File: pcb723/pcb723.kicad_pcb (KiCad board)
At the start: 4 copper layers, 90 x 70 mm, 71 parts, among them J1 Conn_01x02_Pin, J10 Conn_01x05_Socket, J11 Conn_01x05_Socket, J2 Conn_01x02_Pin, J3 Conn_02x07_Odd_Even, J4 Conn_02x02_Odd_Even, J5 USB_C_Receptacle_USB2.0_16P, J6 Conn_02x13_Odd_Even, J7 Conn_02x14_Odd_Even, J8 Conn_02x13_Odd_Even, J9 Conn_02x12_Odd_Even, SW1 SW_Push, U1 STM32H723ZGT6, U2 AMS1117-3.3, Y1 8MHz 20pF

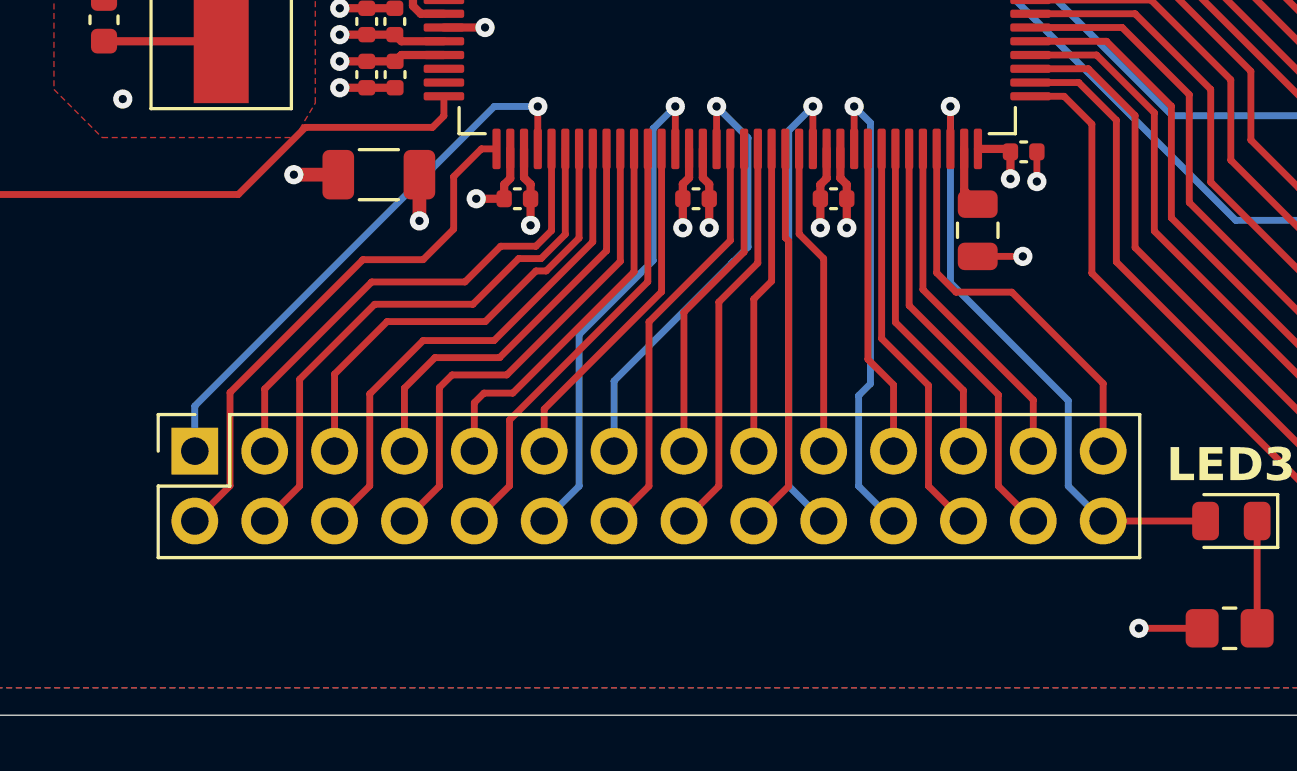
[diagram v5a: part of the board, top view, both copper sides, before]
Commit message: LED3 labels
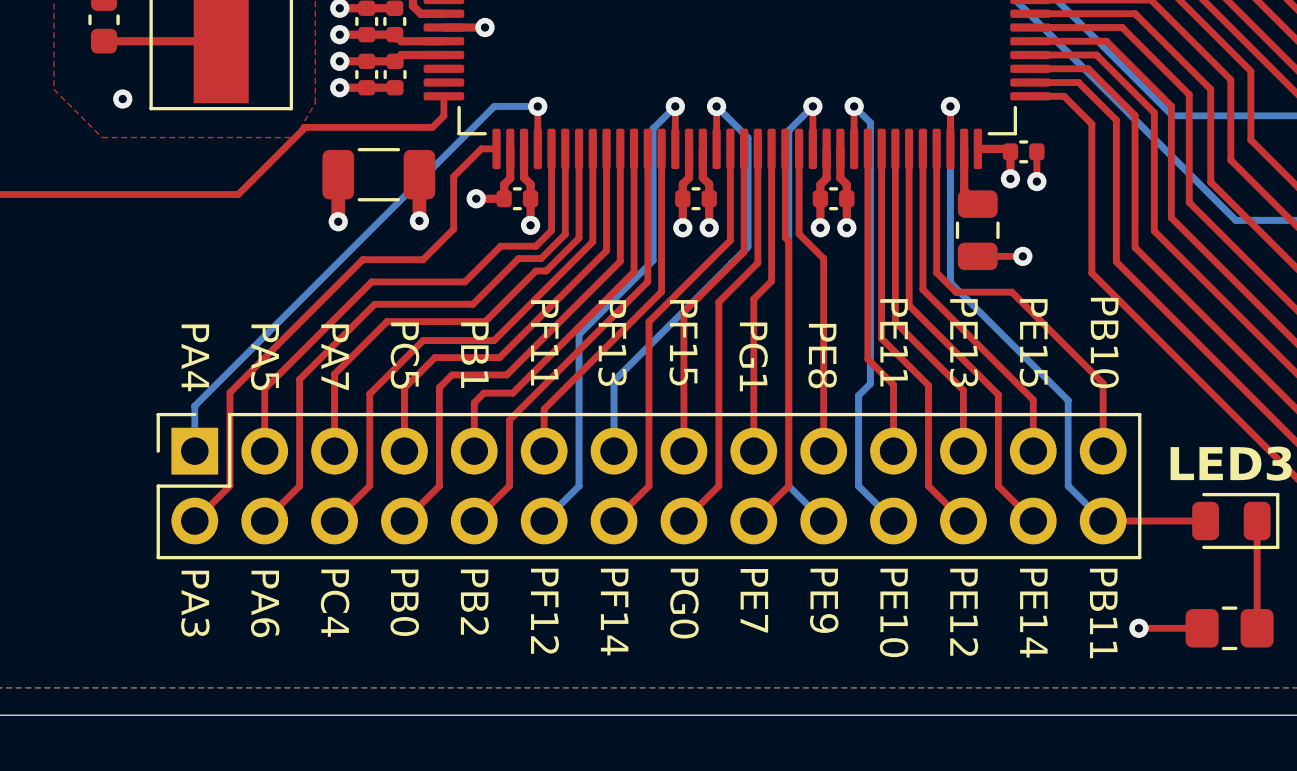
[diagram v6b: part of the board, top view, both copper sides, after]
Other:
- board text added: "PA3"
- board text added: "PA4"
- board text added: "PA5"
- board text added: "PA6"
- board text added: "PA7"
- board text added: "PB0"
- board text added: "PB1"
- board text added: "PB10"
- board text added: "PB11"
- board text added: "PB2"
- board text added: "PC4"
- board text added: "PC5"
- board text added: "PE10"
- board text added: "PE11"
- board text added: "PE12"
- board text added: "PE13"
- board text added: "PE14"
- board text added: "PE15"
- board text added: "PE7"
- board text added: "PE8"
- board text added: "PE9"
- board text added: "PF11"
- board text added: "PF12"
- board text added: "PF13"
- board text added: "PF14"
- board text added: "PF15"
- board text added: "PG0"
- board text added: "PG1"

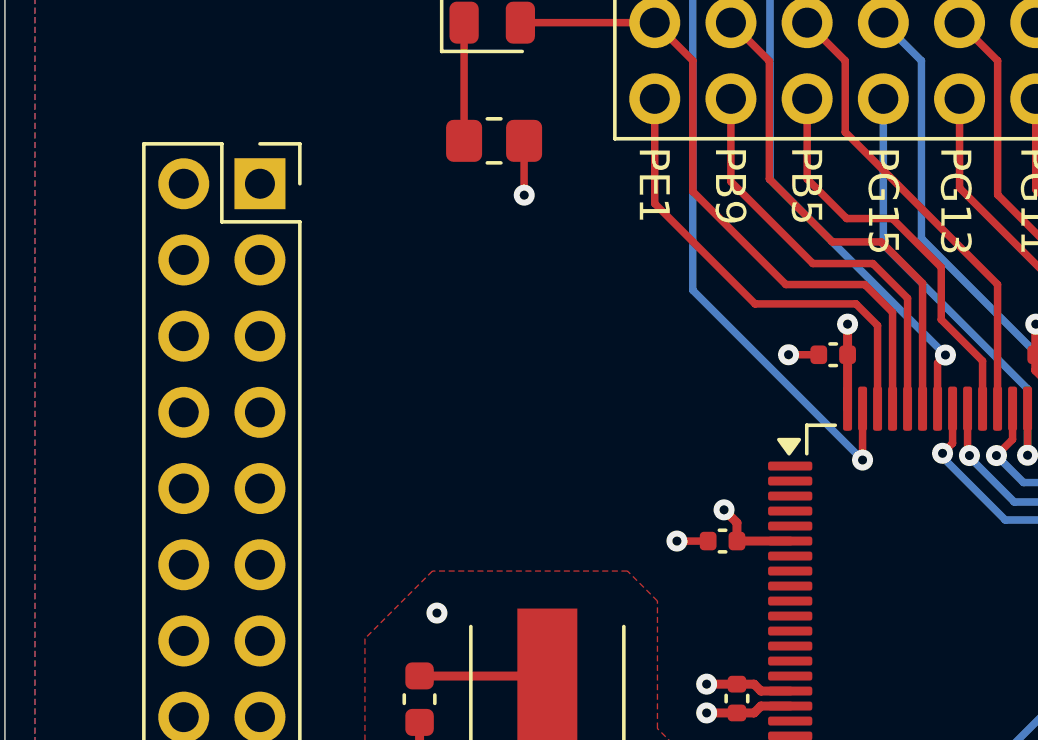
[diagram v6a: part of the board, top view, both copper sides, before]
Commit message: Route LED2 top
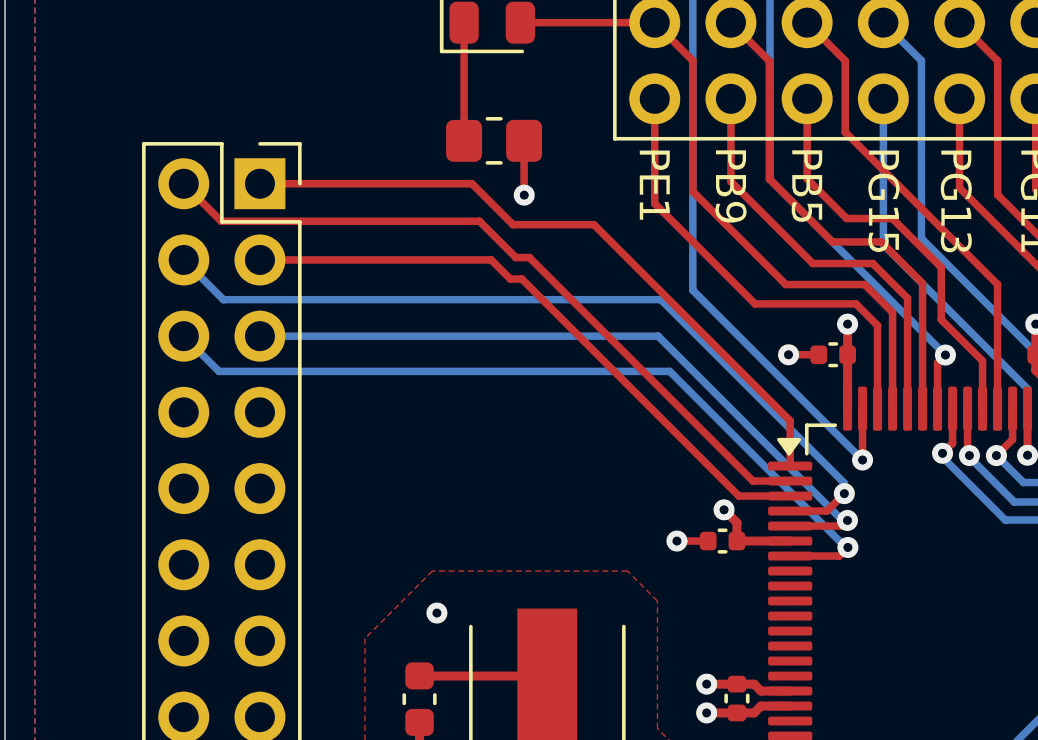
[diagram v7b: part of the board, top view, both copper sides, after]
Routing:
- net /PE5: track 0.00 -> 27.5 mm, vias 0 -> 1
- net /PC13: track 0.00 -> 27.1 mm, vias 0 -> 1
- net /PE3: track 0.00 -> 24.3 mm
- net /PE6: track 0.00 -> 24.1 mm, vias 0 -> 1
- net /PE2: track 0.00 -> 22.5 mm
- net /PE4: track 0.00 -> 20.9 mm

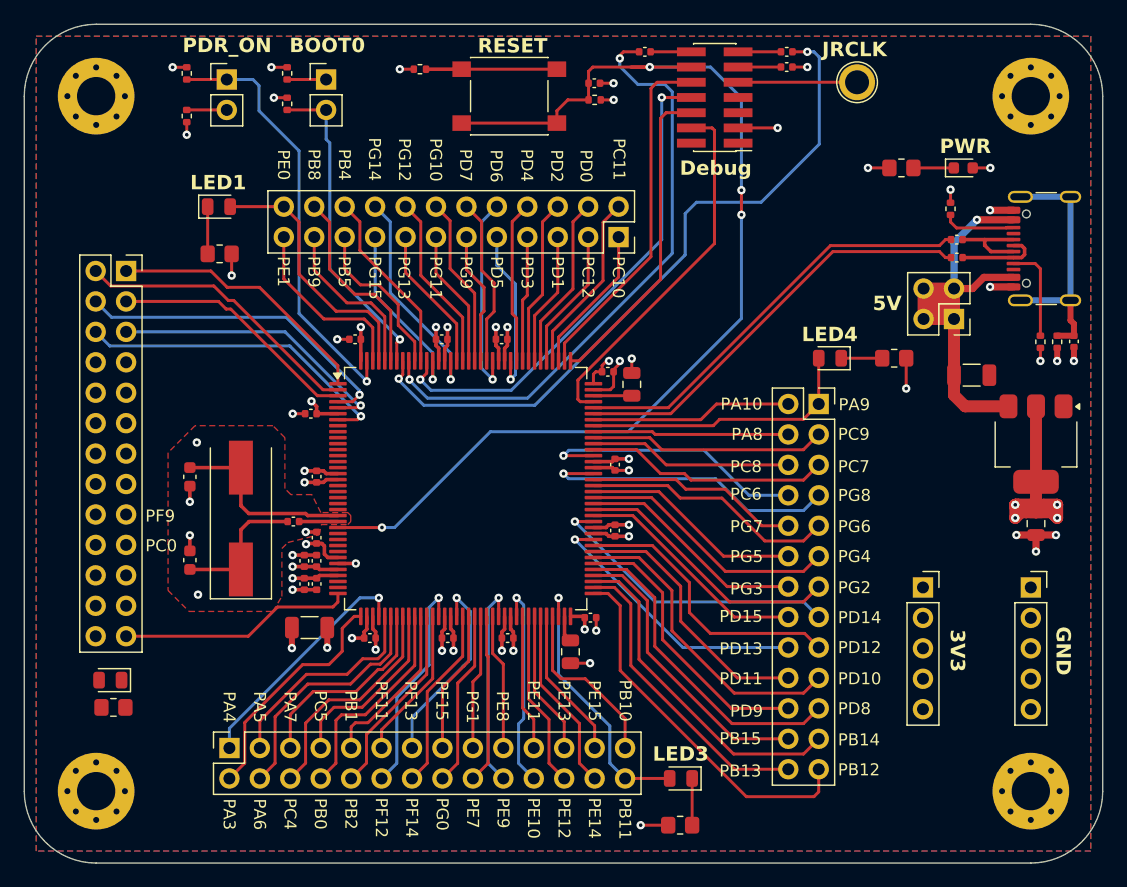
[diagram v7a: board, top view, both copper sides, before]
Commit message: Route LED2
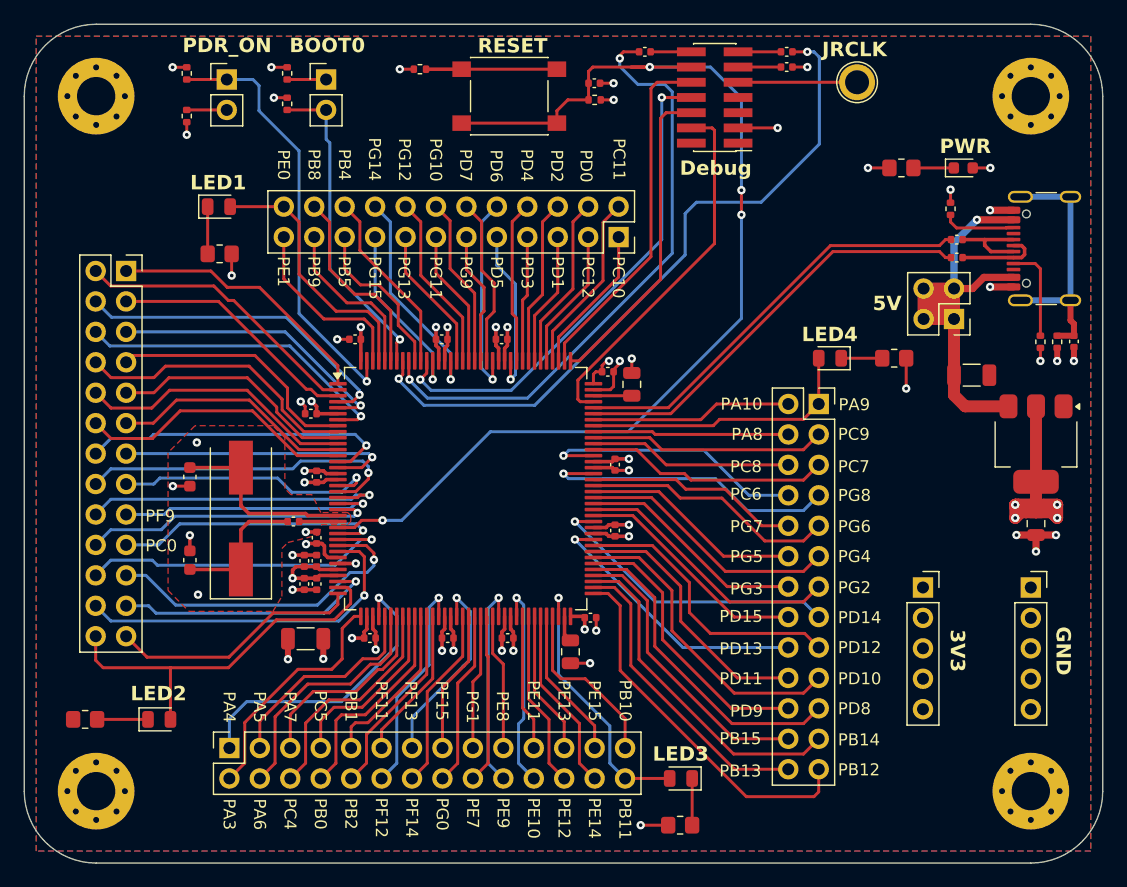
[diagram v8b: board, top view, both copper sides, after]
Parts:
- moved D3 5.23 mm to (101.3, 98.0), turned to 0 degrees
- moved R18 2.56 mm to (95.1, 98.0)
- moved C18 0.99 mm to (113.5, 91.3)
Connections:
- J8 pad 13: /PF4 -> /PF5
- J8 pad 14: /PF5 -> /PF4
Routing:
- net /PA1: track 0.00 -> 32.3 mm
- net /PC3_C: track 0.00 -> 29.5 mm, vias 0 -> 1
- net /PF7: track 0.00 -> 27.8 mm, vias 0 -> 1
- net /PC1: track 0.00 -> 27.4 mm, vias 0 -> 1
- net /PC2_C: track 0.00 -> 27.4 mm, vias 0 -> 1
- net /PF4: track 0.00 -> 26.6 mm, vias 0 -> 1
- net /PF8: track 0.00 -> 26.2 mm, vias 0 -> 1
- net /PF10: track 0.00 -> 24.7 mm, vias 0 -> 1
- net /PC15: track 0.00 -> 23.9 mm
- net /PF5: track 0.00 -> 23.9 mm, vias 0 -> 1
- net /PF3: track 0.00 -> 23.3 mm
- net /PF1: track 0.00 -> 23.2 mm
- net /PC0: track 0.00 -> 22.9 mm, vias 0 -> 1
- net /PF6: track 0.00 -> 22.5 mm, vias 0 -> 1
- net /PF9: track 0.00 -> 22.2 mm, vias 0 -> 1
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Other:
- board text added: "LED2"
